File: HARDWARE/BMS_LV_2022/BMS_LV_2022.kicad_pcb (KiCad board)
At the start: 4 copper layers, 90 x 45 mm, 159 parts, among them J1 Conn_01x06_Male, J11 Conn_01x07_Female, J12 Conn_01x08_Female, J2 Conn_01x12_Male, J3 USB_B_Mini, J4 Battery+, J5 Battery-, Q1 BC846, Q10 BSS138, Q11 SiSS05DN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

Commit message: Small bug fixes
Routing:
- net Net-(C37-Pad2): track 0.00 -> 2.43 mm
- net Net-(C42-Pad1): track 0.00 -> 1.98 mm
- net Net-(C35-Pad2): track 0.00 -> 1.87 mm
- net GND: track 100.6 -> 99.0 mm
- net +5VD: track 88.0 -> 89.4 mm

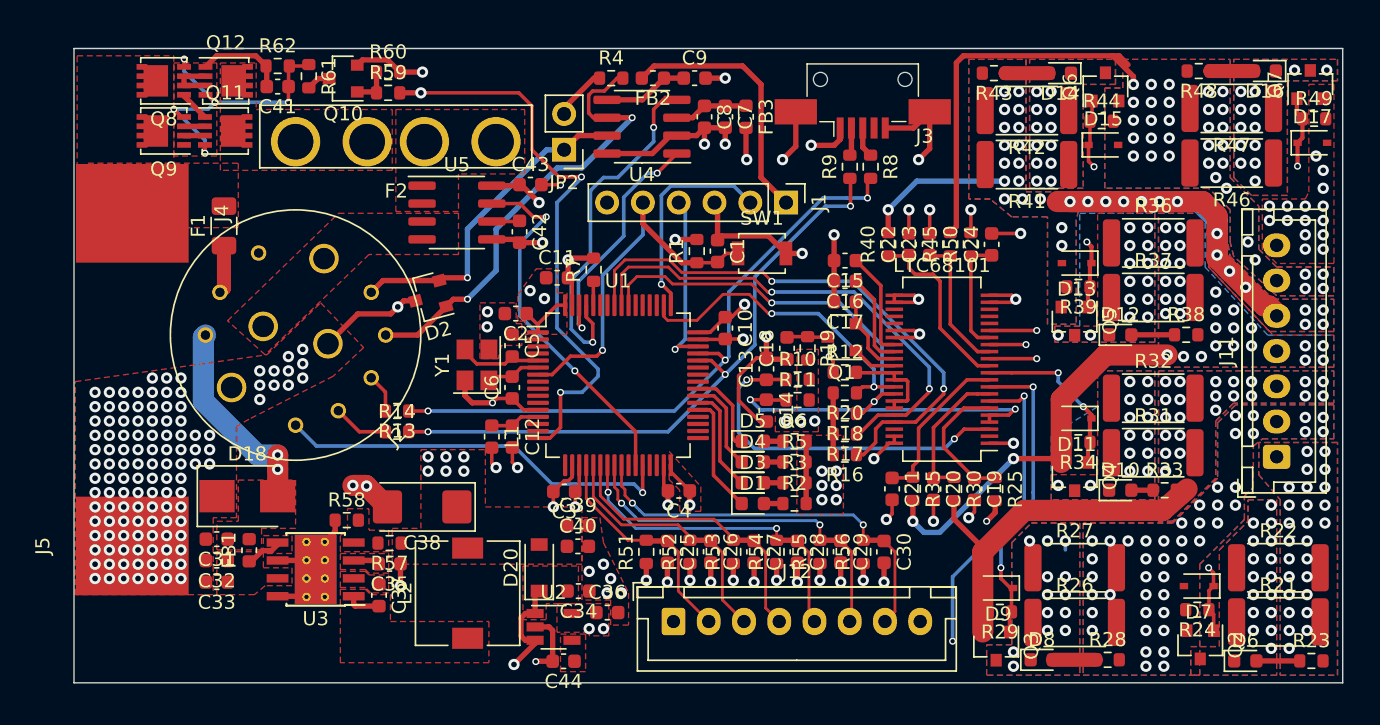
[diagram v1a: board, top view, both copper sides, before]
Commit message: Bug fixes on PCB
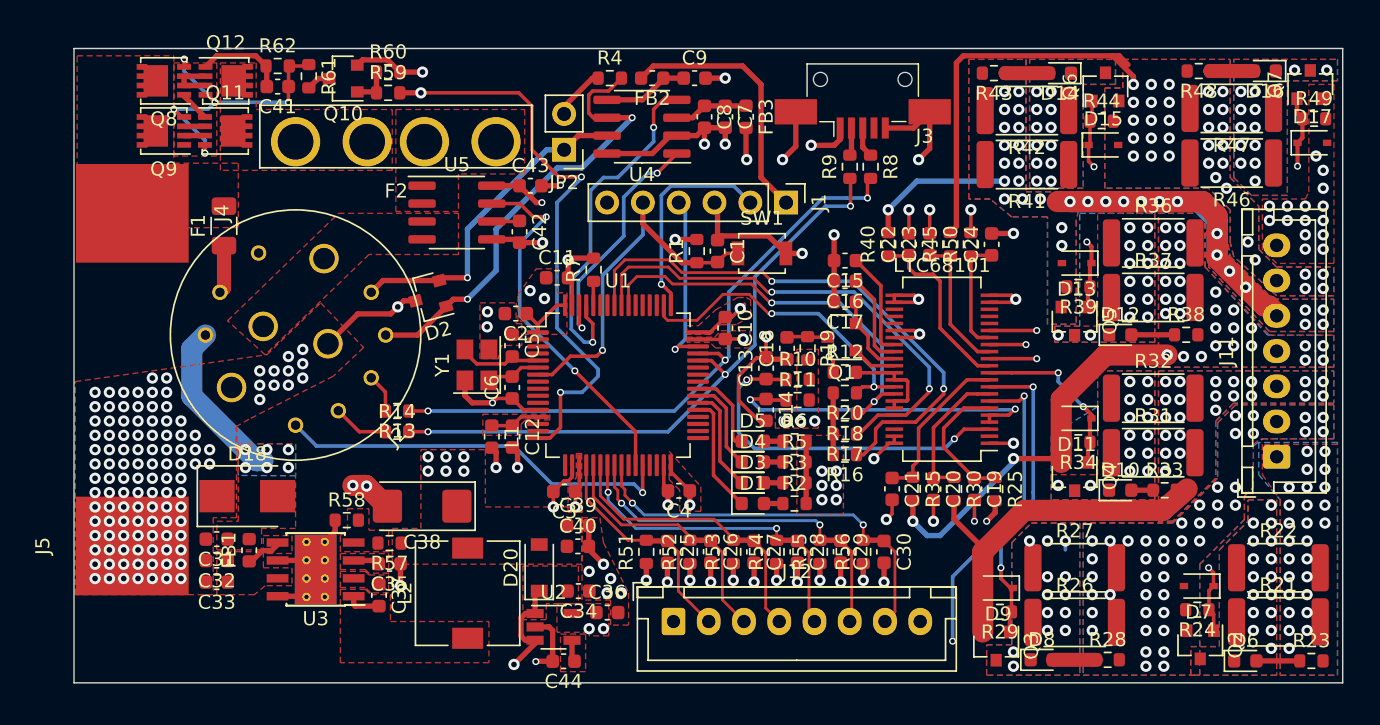
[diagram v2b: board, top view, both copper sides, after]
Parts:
- moved R4 0.10 mm to (148.0, 82.1)
- moved C43 0.08 mm to (142.4, 89.7)
- moved C13 0.06 mm to (159.1, 102.7)
- moved C14 0.06 mm to (159.1, 105.6)
- moved C38 0.05 mm to (134.7, 112.5)
- moved FB2 0.05 mm to (151.0, 82.1)
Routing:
- net GND: track 99.0 -> 102.2 mm, vias 151 -> 147
- net VCC: track 14.5 -> 11.7 mm, vias 2 -> 6
- net Net-(C44-Pad1): track 0.00 -> 1.56 mm
- net GNDPWR: track 43.5 -> 43.0 mm
- added copper zone on F.Cu, net Net-(C12-Pad1)
- added copper zone on B.Cu, net VCC

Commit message: HARDWARE Release V1.0
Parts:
- removed J12: Conn_01x08_Female, Connector_JST:JST_XH_B8B-XH-A_1x08_P2.50mm_Vertical
- added C45: 100nF, Capacitor_SMD:C_0603_1608Metric, F.Cu at (170.0, 115.7)
- added C46: 100nF, Capacitor_SMD:C_0603_1608Metric, F.Cu at (173.1, 115.7)
- added G***: LOGO, Logos:SignatureBox30mm, B.Cu at (158.1, 112.0)
- added G***: LOGO, Logos:PUTM_LOGO_35mm, B.Cu at (159.0, 98.4)
- added J6: Conn_01x09_Female, Connector_JST:JST_XH_B9B-XH-A_1x09_P2.50mm_Vertical, F.Cu at (150.7, 120.9)
- added R15: 1k, Resistor_SMD:R_0603_1608Metric, F.Cu at (128.8, 108.5)
- added R63: 10k, Resistor_SMD:R_0603_1608Metric, F.Cu at (168.5, 115.7)
- added R64: 10k, Resistor_SMD:R_0603_1608Metric, F.Cu at (171.6, 115.7)
- moved C36 1.19 mm to (147.0, 120.8), turned to 270 degrees
- moved C25 0.51 mm to (151.6, 115.7)
- moved C26 0.51 mm to (154.7, 115.7)
- moved C28 0.51 mm to (160.8, 115.7)
- moved C29 0.51 mm to (163.9, 115.7)
- moved C30 0.51 mm to (167.0, 115.7)
- moved R52 0.51 mm to (153.2, 115.7)
- moved R53 0.51 mm to (156.3, 115.7)
- moved R55 0.51 mm to (162.4, 115.7)
- moved R56 0.51 mm to (165.5, 115.7)
- moved C27 0.51 mm to (157.7, 115.7)
- moved R51 0.51 mm to (150.1, 115.7)
- moved R54 0.51 mm to (159.3, 115.7)
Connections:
- C13 pad 2: GNDPWR -> GND
- C14 pad 2: GNDPWR -> GND
- C15 pad 2: GNDPWR -> GND
- C16 pad 2: GNDPWR -> GND
- C17 pad 2: GNDPWR -> GND
- C18 pad 1: GNDPWR -> GND
- C19 pad 2: GNDPWR -> GND
- C20 pad 2: GNDPWR -> GND
- C21 pad 2: GNDPWR -> GND
- C22 pad 2: GNDPWR -> GND
- C23 pad 2: GNDPWR -> GND
- C24 pad 2: GNDPWR -> GND
- D17 pad 2: GNDPWR -> GND
- J11 pad 7: GNDPWR -> GND
- J2 pad 5: /Interlock -> Net-(J2-Pad5)
- LTC68101 pad 1: GNDPWR -> GND
- LTC68101 pad 21: GNDPWR -> GND
- LTC68101 pad 22: GNDPWR -> GND
- LTC68101 pad 23: GNDPWR -> GND
- LTC68101 pad 24: GNDPWR -> GND
- LTC68101 pad 28: GNDPWR -> GND
- LTC68101 pad 29: GNDPWR -> GND
- LTC68101 pad 43: GNDPWR -> GND
- LTC68101 pad 44: GNDPWR -> GND
- Q7 pad 2: GNDPWR -> GND
- R12 pad 1: GNDPWR -> GND
- R49 pad 2: GNDPWR -> GND
- R50 pad 2: GNDPWR -> GND
- U1 pad 17: Net-(U1-Pad17) -> /Therm_1
- U1 pad 20: /Therm_1 -> /Therm_2
- U1 pad 21: /Therm_2 -> /Therm_3
- U1 pad 22: /Therm_3 -> /Therm_4
- U1 pad 23: /Therm_4 -> /Therm_5
- U1 pad 24: /Therm_5 -> /Therm_6
- U1 pad 25: /Therm_6 -> /Therm_7
- U1 pad 26: Net-(U1-Pad26) -> /Therm_8
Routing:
- net GNDPWR: track 43.0 -> 0.00 mm, vias 30 -> 0
- net /Therm_8: track 0.00 -> 39.3 mm, vias 0 -> 2
- net GND: track 102.2 -> 137.4 mm, vias 147 -> 257
- net /Therm_7: track 0.00 -> 34.1 mm, vias 0 -> 2
- net /Therm_1: track 16.3 -> 20.3 mm, vias 0 -> 2
- net Net-(J2-Pad5): track 0.00 -> 3.00 mm
- net /Therm_5: track 26.3 -> 29.3 mm
- net /Therm_6: track 28.9 -> 31.7 mm
- net +3V3: track 53.2 -> 55.8 mm
- net /LTC6810/CellBalance4: track 28.2 -> 26.7 mm
- net /Therm_3: track 20.9 -> 22.4 mm
- net /Therm_4: track 23.9 -> 25.1 mm, vias 2 -> 0
- net +5VD: track 89.4 -> 88.7 mm
- net /Therm_2: track 18.7 -> 19.4 mm
- net +5V: track 45.2 -> 44.6 mm
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- added copper zone on In1.Cu, net +24V
- added copper zone on In1.Cu, net /CS_IP+
- added copper zone on In1.Cu, net /LTC6810/CellBalance3
- added copper zone on In1.Cu, net /LTC6810/CellBalance4
- added copper zone on In1.Cu, net /LTC6810/CellBalance5
- added copper zone on In1.Cu, net /LTC6810/CellBalance6
- added copper zone on In1.Cu, net /V_Out
- added copper zone on In1.Cu, net Net-(D10-Pad1)
- added copper zone on In1.Cu, net Net-(D12-Pad1)
- added copper zone on In1.Cu, net Net-(D14-Pad1)
- added copper zone on In1.Cu, net Net-(D16-Pad1)
- added copper zone on In1.Cu, net Net-(D6-Pad1)
- added copper zone on In1.Cu, net Net-(D8-Pad1)
- added copper zone on In1.Cu, net Net-(F2-Pad2)
- removed copper zone on F.Cu, net GNDPWR
- removed copper zone on In2.Cu, net GNDPWR
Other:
- board text added: ""To mały krok dla ludzkości, ale dla karła normalny" Sebek Bąk"
- board text added: "BATT"
- board text added: "Battery Management System"
- board text added: "GND"
- board text added: "Maksymilian Jaruga"
- board text added: "Szymon Sambor"
- board text added: "Therm_1"
